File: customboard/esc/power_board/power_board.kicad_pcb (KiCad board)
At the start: 4 copper layers, 44 x 46.5 mm, 107 parts, among them J1 Conn_01x08_MountingPin, J10 Conn_01x03_Pin, J2 Conn_01x01, J3 Conn_01x01, J4 Conn_01x03_Pin, J5 Conn_01x03_Pin, J6 Conn_01x03_Pin, Q1 BSC010N04LS6, Q10 BSC010N04LS6, Q11 BSC010N04LS6, Q12 BSC010N04LS6, Q13 BSC010N04LS6, Q14 BSC010N04LS6, Q15 BSC010N04LS6, Q16 BSC010N04LS6, Q17 BSC010N04LS6, Q18 BSC010N04LS6, Q19 BSC010N04LS6, Q2 BSC010N04LS6, Q20 BSC010N04LS6, Q21 BSC010N04LS6, Q22 BSC010N04LS6, Q23 BSC010N04LS6, Q24 BSC010N04LS6, Q3 BSC010N04LS6, Q4 BSC010N04LS6, Q5 BSC010N04LS6, Q6 BSC010N04LS6, Q7 BSC010N04LS6, Q8 BSC010N04LS6, Q9 BSC010N04LS6, U2 AP130-25Y, U3 AP7381-33SA-7, U4 AP130-25Y, U5 AP130-25Y, U7 AP7381-33SA-7, U8 AP130-25Y

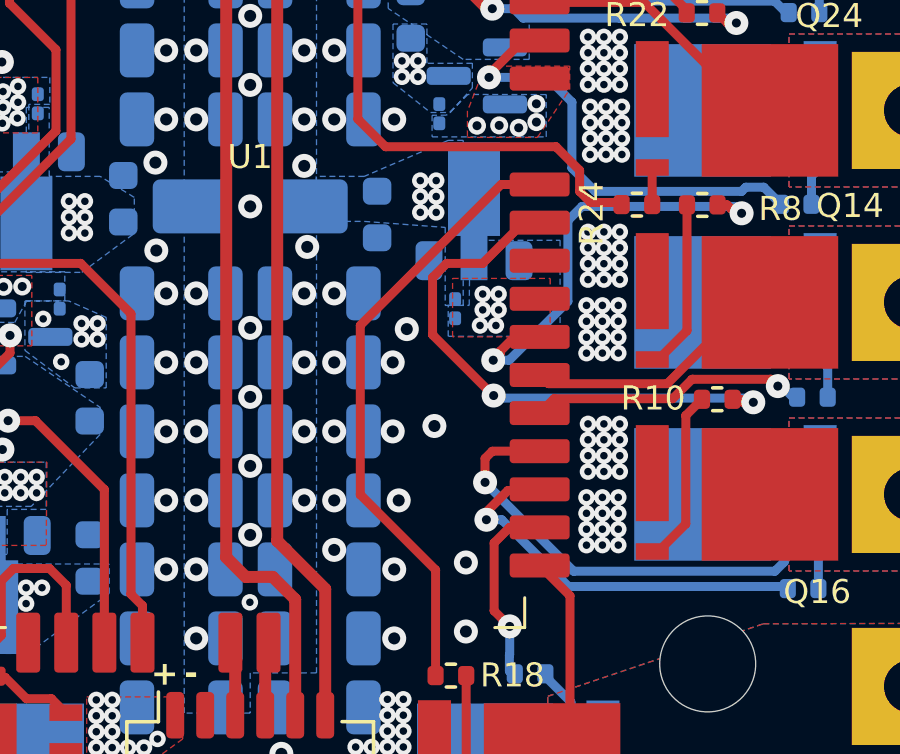
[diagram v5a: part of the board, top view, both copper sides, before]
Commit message: narrower castelations on logic board; proper stls
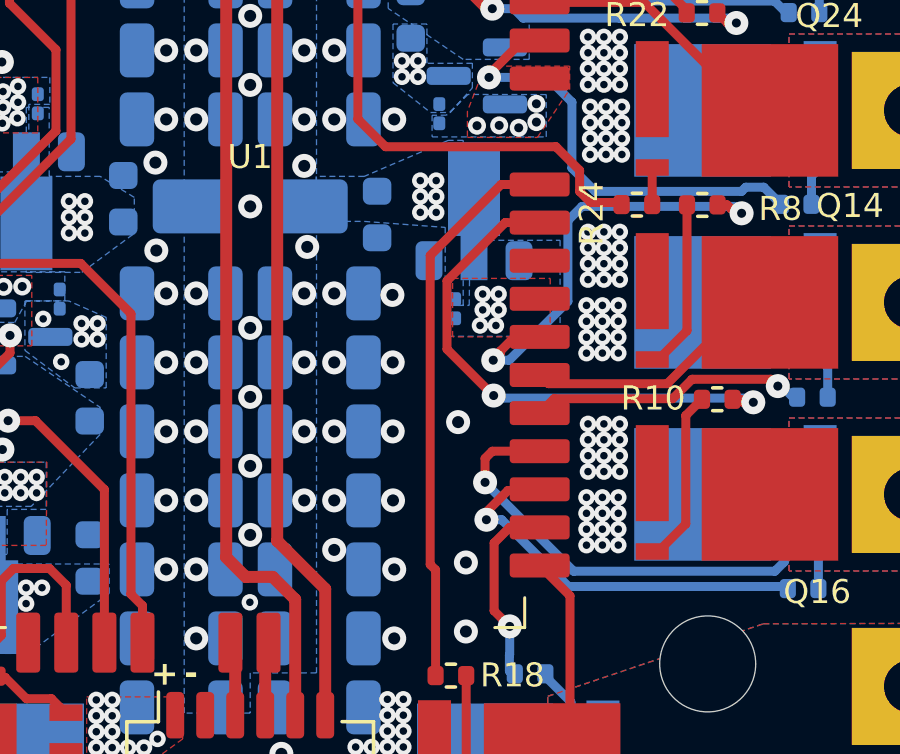
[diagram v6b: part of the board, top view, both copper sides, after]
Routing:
- net /EscMotor3/GLA: track 20.6 -> 18.7 mm
- net /EscMotor3/GLB: track 18.6 -> 17.8 mm
- net GND: vias 208 -> 207
- net +BATT: vias 173 -> 174
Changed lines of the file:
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@@
 		(sheetname "/")
 		(sheetfile "power_board.kicad_sch")
-		(attr smd)
+		(attr smd exclude_from_bom)
 		(fp_line
 			(start -9.15 -13.04)
@@
 		(model "${KIPRJMOD}/components/3dmodels/logic_board.step"
 			(offset
-				(xyz -54.5 -8.325 1.55)
+				(xyz -9.15 -14.05 0)
 			)
 			(scale
@@
 		(sheetname "/")
 		(sheetfile "power_board.kicad_sch")
-		(attr exclude_from_pos_files)
+		(attr exclude_from_pos_files exclude_from_bom)
 		(fp_circle
 			(center 0 0)
@@
 		(sheetname "/")
 		(sheetfile "power_board.kicad_sch")
-		(attr exclude_from_pos_files)
+		(attr exclude_from_pos_files exclude_from_bom)
 		(fp_circle
 			(center 0 0)
@@
 	)
 	(via
-		(at 156.14 107.32)
+		(at 156.93 107.19)
 		(size 0.8)
 		(drill 0.4)
@@
 	)
 	(via
-		(at 155.22 104.09)
-		(size 0.8)
-		(drill 0.4)
-		(layers "F.Cu" "B.Cu")
-		(free yes)
-		(net 1)
-	)
-	(via
 		(at 143.87 121.45)
 		(size 0.55)
@@
 	)
 	(via
+		(at 154.74 102.95)
+		(size 0.8)
+		(drill 0.4)
+		(layers "F.Cu" "B.Cu")
+		(free yes)
+		(net 2)
+	)
+	(via
 		(at 147.2 85.6)
 		(size 0.8)
@@
 	)
 	(via
-		(at 154.95 109.8)
+		(at 154.76 109.8)
 		(size 0.8)
 		(drill 0.4)
@@
 	)
 	(segment
-		(start 158.105315 106.305315)
-		(end 156.08 104.28)
+		(start 156.56 104.76)
+		(end 156.56 102.48)
 		(width 0.3)
 		(layer "F.Cu")
@@
 	)
 	(segment
-		(start 156.55 101.9)
-		(end 157.75 101.9)
+		(start 158.105315 106.305315)
+		(end 156.56 104.76)
 		(width 0.3)
 		(layer "F.Cu")
@@
 	)
 	(segment
-		(start 158.115199 106.305315)
-		(end 158.105315 106.305315)
-		(width 0.3)
-		(layer "F.Cu")
-		(net 58)
-	)
-	(segment
-		(start 159.11 100.54)
+		(start 158.5 100.54)
 		(end 159.65 100.54)
 		(width 0.3)
@@
 	)
 	(segment
-		(start 156.08 104.28)
-		(end 156.08 102.37)
-		(width 0.3)
-		(layer "F.Cu")
-		(net 58)
-	)
-	(segment
 		(start 166.77 106.53)
 		(end 166.43 106.53)
@@
 	)
 	(segment
-		(start 156.08 102.37)
-		(end 156.55 101.9)
+		(start 156.56 102.48)
+		(end 158.5 100.54)
 		(width 0.3)
 		(layer "F.Cu")
@@
 	)
 	(segment
-		(start 157.75 101.9)
-		(end 159.11 100.54)
+		(start 158.115199 106.305315)
+		(end 158.105315 106.305315)
 		(width 0.3)
 		(layer "F.Cu")
@@
 	)
 	(segment
-		(start 153.67 103.965298)
-		(end 158.365298 99.27)
-		(width 0.3)
-		(layer "F.Cu")
-		(net 60)
-	)
-	(segment
-		(start 153.67 109.61)
-		(end 153.67 103.965298)
+		(start 156 111.937925)
+		(end 156 101.635298)
 		(width 0.3)
 		(layer "F.Cu")
@@
 	)
 	(segment
-		(start 156.18 115.64)
-		(end 156.18 112.117925)
+		(start 156.18 112.117925)
+		(end 156 111.937925)
 		(width 0.3)
 		(layer "F.Cu")
@@
 	)
 	(segment
-		(start 156.18 112.117925)
-		(end 153.672075 109.61)
+		(start 156 101.635298)
+		(end 158.365298 99.27)
 		(width 0.3)
 		(layer "F.Cu")
@@
 	)
 	(segment
-		(start 153.672075 109.61)
-		(end 153.67 109.61)
+		(start 156.18 115.64)
+		(end 156.18 112.117925)
 		(width 0.3)
 		(layer "F.Cu")
